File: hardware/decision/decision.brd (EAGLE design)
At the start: 45 x 70 mm, 8 parts, among them IC1 7805T, IC2 A1301UA

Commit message: update decision board with proper nets
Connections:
- removed net N$1: GND.1, GND.2, GND.3
- removed net N$2: VCC.1, VCC.2, VCC.3
- net GND: now also GND.1, GND.2, GND.3
- net VCC: now also VCC.1, VCC.2, VCC.3
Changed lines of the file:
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@@
 <contactref element="IC2" pad="2"/>
 <via x="2.54" y="13.97" extent="1-16" drill="1.4" diameter="2.54" shape="square"/>
+<contactref element="GND" pad="3"/>
+<contactref element="GND" pad="2"/>
+<contactref element="GND" pad="1"/>
 <wire x1="10.89" y1="18.86" x2="12.86" y2="53.51" width="0" layer="19" extent="1-1"/>
 <wire x1="2.54" y1="13.97" x2="10.89" y2="18.86" width="0" layer="19" extent="1-1"/>
 <wire x1="7.62" y1="6.35" x2="2.54" y2="13.97" width="0" layer="19" extent="1-1"/>
 <wire x1="13.97" y1="6.35" x2="7.62" y2="6.35" width="0" layer="19" extent="1-1"/>
+<wire x1="26.563" y1="6.41" x2="13.97" y2="6.35" width="0" layer="19" extent="1-1"/>
+<wire x1="26.817" y1="8.95" x2="26.563" y2="6.41" width="0" layer="19" extent="1-1"/>
+<wire x1="26.817" y1="3.87" x2="26.563" y2="6.41" width="0" layer="19" extent="1-1"/>
 </signal>
 <signal name="VCC">
@@
 <contactref element="C2" pad="1"/>
 <contactref element="IC2" pad="1"/>
+<contactref element="VCC" pad="1"/>
+<contactref element="VCC" pad="3"/>
+<contactref element="VCC" pad="2"/>
+<wire x1="13.43" y1="18.86" x2="12.86" y2="52.24" width="0" layer="19" extent="1-1"/>
 <wire x1="16.51" y1="6.35" x2="13.43" y2="18.86" width="0" layer="19" extent="1-1"/>
-<wire x1="12.86" y1="52.24" x2="16.51" y2="6.35" width="0" layer="19" extent="1-1"/>
+<wire x1="39.563" y1="6.49" x2="16.51" y2="6.35" width="0" layer="19" extent="1-1"/>
+<wire x1="39.817" y1="9.03" x2="39.563" y2="6.49" width="0" layer="19" extent="1-1"/>
+<wire x1="39.817" y1="3.95" x2="39.563" y2="6.49" width="0" layer="19" extent="1-1"/>
 </signal>
 <signal name="P1.2">
@@
 <wire x1="5.08" y1="6.35" x2="8.35" y2="18.86" width="0" layer="19" extent="1-1"/>
 </signal>
-<signal name="N$1">
-<contactref element="GND" pad="3"/>
-<contactref element="GND" pad="2"/>
-<contactref element="GND" pad="1"/>
-<wire x1="26.563" y1="6.41" x2="26.817" y2="8.95" width="0" layer="19" extent="1-1"/>
-<wire x1="26.817" y1="3.87" x2="26.563" y2="6.41" width="0" layer="19" extent="1-1"/>
-</signal>
-<signal name="N$2">
-<contactref element="VCC" pad="1"/>
-<contactref element="VCC" pad="3"/>
-<contactref element="VCC" pad="2"/>
-<wire x1="39.563" y1="6.49" x2="39.817" y2="9.03" width="0" layer="19" extent="1-1"/>
-<wire x1="39.817" y1="3.95" x2="39.563" y2="6.49" width="0" layer="19" extent="1-1"/>
-</signal>
 </signals>

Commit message: working on decision board traces
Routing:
- net N$3: track 0.00 -> 49.0 mm
- net N$5: track 0.00 -> 39.3 mm
- net N$2: track 0.00 -> 19.2 mm
- net N$1: track 0.00 -> 18.8 mm
- net N$4: track 0.00 -> 13.2 mm
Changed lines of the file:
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@@
 </signal>
 <signal name="9V">
-<via x="2.54" y="19.05" extent="1-16" drill="1.4" diameter="2.54" shape="square"/>
+<via x="2.54" y="18.05" extent="1-16" drill="1.4" diameter="2.54" shape="square"/>
 <contactref element="IC1" pad="1"/>
 <contactref element="C1" pad="2"/>
-<wire x1="2.54" y1="19.05" x2="8.35" y2="18.86" width="0" layer="19" extent="1-1"/>
+<wire x1="2.54" y1="18.05" x2="8.35" y2="18.86" width="0" layer="19" extent="1-1"/>
 <wire x1="5.08" y1="6.35" x2="8.35" y2="18.86" width="0" layer="19" extent="1-1"/>
 </signal>
+<signal name="N$3">
+<wire x1="13" y1="55" x2="13" y2="56" width="0.6096" layer="16"/>
+<wire x1="13" y1="56" x2="25" y2="68" width="0.6096" layer="16"/>
+<wire x1="25" y1="68" x2="40" y2="68" width="0.6096" layer="16"/>
+<wire x1="40" y1="68" x2="42" y2="66" width="0.6096" layer="16"/>
+<wire x1="42" y1="66" x2="42" y2="57" width="0.6096" layer="16"/>
+<wire x1="42" y1="57" x2="39" y2="54" width="0.6096" layer="16"/>
+</signal>
+<signal name="N$1">
+<wire x1="8" y1="18" x2="7" y2="18" width="0.8128" layer="16"/>
+<wire x1="7" y1="18" x2="5" y2="16" width="0.8128" layer="16"/>
+<wire x1="5" y1="16" x2="5" y2="6" width="0.8128" layer="16"/>
+<wire x1="7" y1="18" x2="2" y2="18" width="0.8128" layer="16"/>
+</signal>
+<signal name="N$2">
+<wire x1="11" y1="18" x2="11" y2="17" width="0.8128" layer="1"/>
+<wire x1="11" y1="17" x2="8" y2="14" width="0.8128" layer="1"/>
+<wire x1="8" y1="14" x2="2" y2="14" width="0.8128" layer="1"/>
+<wire x1="8" y1="14" x2="8" y2="6" width="0.8128" layer="1"/>
+</signal>
+<signal name="N$4">
+<wire x1="13" y1="18" x2="13" y2="13" width="0.8128" layer="1"/>
+<wire x1="13" y1="13" x2="16" y2="10" width="0.8128" layer="1"/>
+<wire x1="16" y1="10" x2="16" y2="6" width="0.8128" layer="1"/>
+</signal>
+<signal name="N$5">
+<wire x1="13" y1="20" x2="17" y2="20" width="0.6096" layer="1"/>
+<wire x1="17" y1="20" x2="19" y2="22" width="0.6096" layer="1"/>
+<wire x1="19" y1="22" x2="19" y2="46" width="0.6096" layer="1"/>
+<wire x1="19" y1="46" x2="13" y2="52" width="0.6096" layer="1"/>
+</signal>
 </signals>

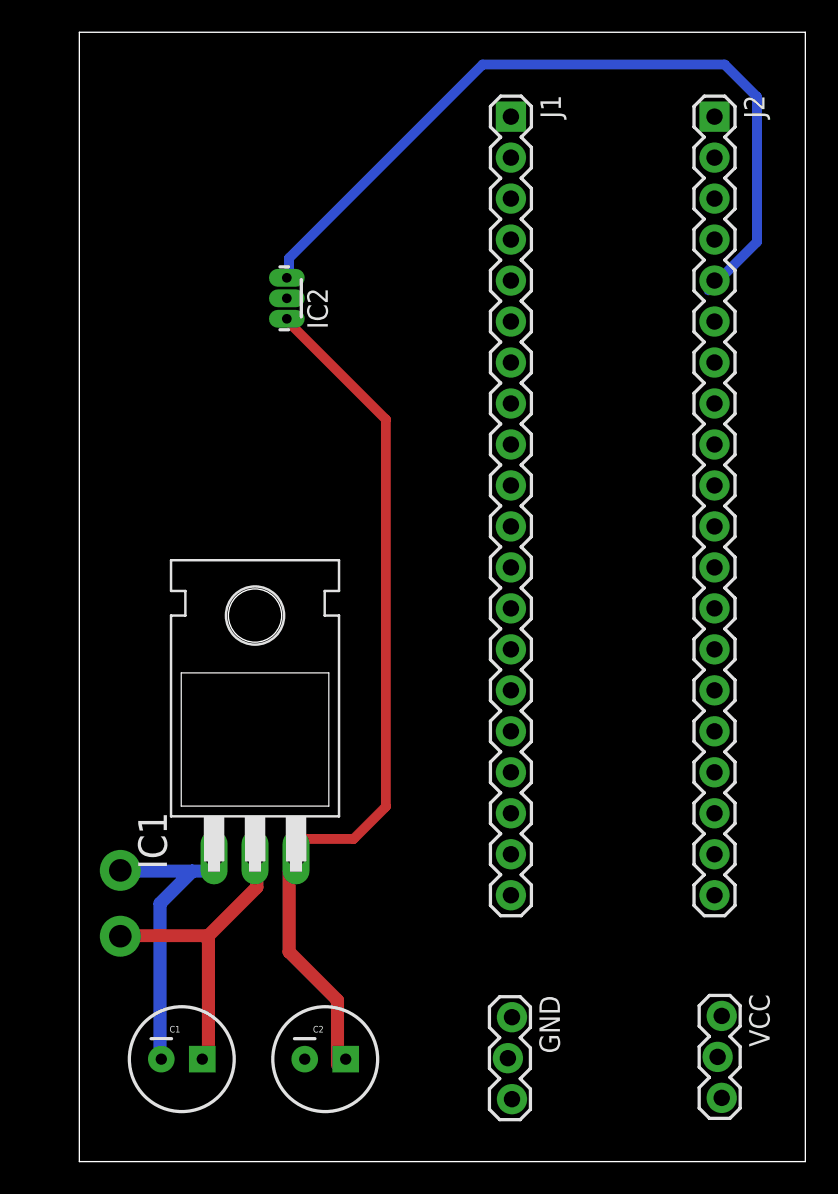
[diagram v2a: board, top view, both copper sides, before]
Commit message: update decision board with copper pools, silk screen, and proper routes
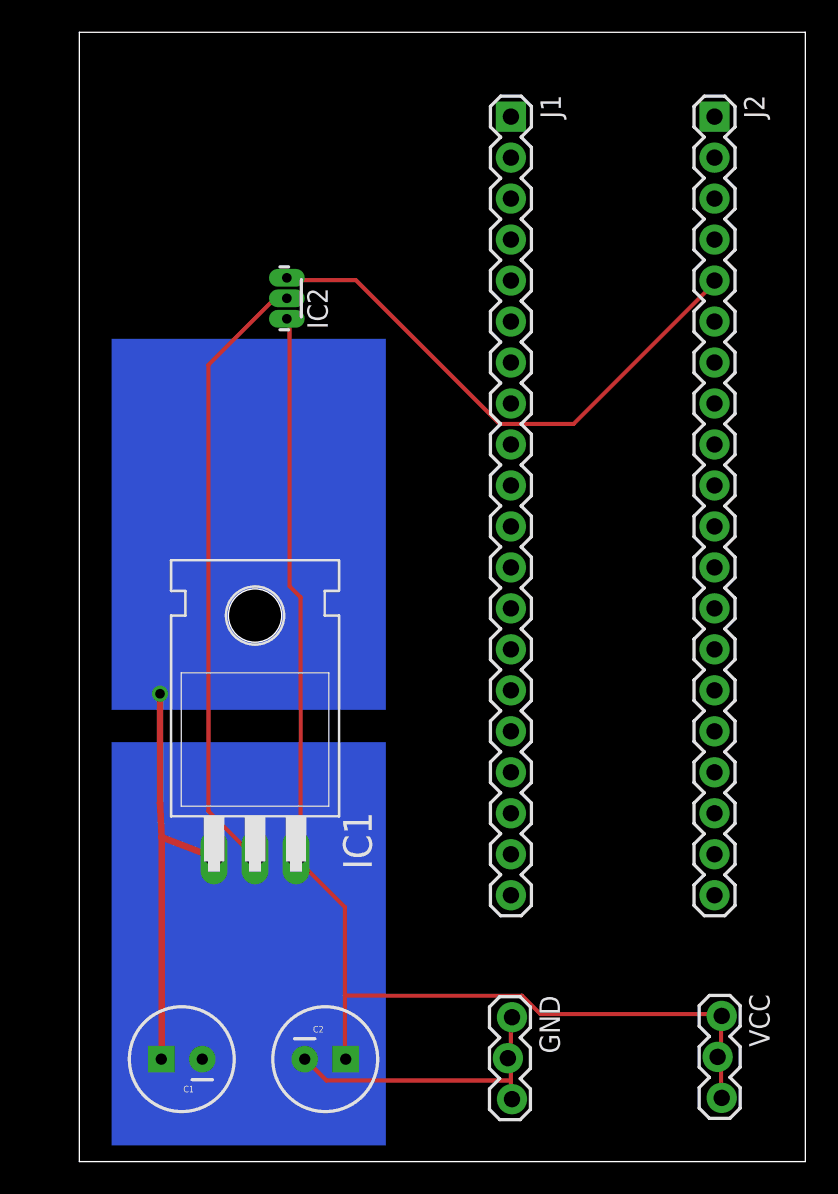
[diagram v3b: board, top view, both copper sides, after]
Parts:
- turned C1 to 180 degrees
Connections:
- net 9V: now also C1.1; no longer C1.2
- net GND: now also C1.2; no longer C1.1
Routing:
- net VCC: track 0.00 -> 76.9 mm
- net GND: track 0.00 -> 75.4 mm, vias 1 -> 0
- net N$3: track 49.0 -> 0.00 mm
- net N$5: track 39.3 -> 0.00 mm
- net P1.2: track 0.00 -> 34.0 mm
- net 9V: track 0.00 -> 26.1 mm
- net N$2: track 19.2 -> 0.00 mm
- net N$1: track 18.8 -> 0.00 mm
- net N$4: track 13.2 -> 0.00 mm
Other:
- board text added: "Decision Board"
- board text added: "Derailleurs"
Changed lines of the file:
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@@
 <wire x1="45" y1="70" x2="0" y2="70" width="0" layer="20"/>
 <wire x1="0" y1="70" x2="0" y2="0" width="0" layer="20"/>
+<rectangle x1="2" y1="1" x2="19" y2="26" layer="16"/>
+<text x="2" y="67" size="1.778" layer="48">Decision Board</text>
+<text x="2" y="64" size="1.778" layer="48">Derailleurs</text>
+<rectangle x1="2" y1="28" x2="19" y2="51" layer="16"/>
 </plain>
 <attributes>
@@
 <param name="RoutingGrid" value="50mil"/>
 <param name="AutoGrid" value="1"/>
-<param name="Efforts" value="0"/>
+<param name="Efforts" value="2"/>
 <param name="TopRouterVariant" value="1"/>
 <param name="tpViaShape" value="round"/>
@@
 </autorouter>
 <elements>
-<element name="C1" library="SparkFun-Capacitors" package="CPOL-RADIAL-100UF-25V" value="200µF" x="6.35" y="6.35"/>
+<element name="C1" library="SparkFun-Capacitors" package="CPOL-RADIAL-100UF-25V" value="200µF" x="6.35" y="6.35" rot="R180"/>
 <element name="C2" library="SparkFun-Capacitors" package="CPOL-RADIAL-100UF-25V" value="200µF" x="15.24" y="6.35"/>
 <element name="IC1" library="linear" package="TO220H" value="7805T" x="10.89" y="29.02"/>
@@
 <signal name="GND">
 <contactref element="IC1" pad="2"/>
-<contactref element="C1" pad="1"/>
+<contactref element="C1" pad="2"/>
 <contactref element="C2" pad="2"/>
 <contactref element="IC2" pad="2"/>
-<via x="2.54" y="13.97" extent="1-16" drill="1.4" diameter="2.54" shape="square"/>
 <contactref element="GND" pad="3"/>
 <contactref element="GND" pad="2"/>
 <contactref element="GND" pad="1"/>
-<wire x1="10.89" y1="18.86" x2="12.86" y2="53.51" width="0" layer="19" extent="1-1"/>
-<wire x1="2.54" y1="13.97" x2="10.89" y2="18.86" width="0" layer="19" extent="1-1"/>
-<wire x1="7.62" y1="6.35" x2="2.54" y2="13.97" width="0" layer="19" extent="1-1"/>
-<wire x1="13.97" y1="6.35" x2="7.62" y2="6.35" width="0" layer="19" extent="1-1"/>
-<wire x1="26.563" y1="6.41" x2="13.97" y2="6.35" width="0" layer="19" extent="1-1"/>
-<wire x1="26.817" y1="8.95" x2="26.563" y2="6.41" width="0" layer="19" extent="1-1"/>
-<wire x1="26.817" y1="3.87" x2="26.563" y2="6.41" width="0" layer="19" extent="1-1"/>
+<wire x1="10.89" y1="18.86" x2="10.89" y2="9.43" width="0.4064" layer="16"/>
+<wire x1="10.89" y1="9.43" x2="13.97" y2="6.35" width="0.4064" layer="16"/>
+<wire x1="10.89" y1="9.43" x2="10.7" y2="9.43" width="0.4064" layer="16"/>
+<wire x1="10.7" y1="9.43" x2="7.62" y2="6.35" width="0.4064" layer="16"/>
+<wire x1="26.7462" y1="8.9154" x2="26.7462" y2="6.6294" width="0.254" layer="1"/>
+<wire x1="26.7462" y1="6.6294" x2="26.563" y2="6.41" width="0.254" layer="1"/>
+<wire x1="26.7462" y1="8.9154" x2="26.817" y2="8.95" width="0.254" layer="1"/>
+<wire x1="26.7462" y1="6.4008" x2="26.7462" y2="5.0292" width="0.254" layer="1"/>
+<wire x1="26.7462" y1="5.0292" x2="26.7462" y2="3.8862" width="0.254" layer="1"/>
+<wire x1="26.7462" y1="3.8862" x2="26.817" y2="3.87" width="0.254" layer="1"/>
+<wire x1="26.7462" y1="6.4008" x2="26.563" y2="6.41" width="0.254" layer="1"/>
+<wire x1="12.1158" y1="53.4924" x2="12.8016" y2="53.4924" width="0.254" layer="1"/>
+<wire x1="8.001" y1="49.3776" x2="12.1158" y2="53.4924" width="0.254" layer="1"/>
+<wire x1="8.001" y1="21.717" x2="8.001" y2="49.3776" width="0.254" layer="1"/>
+<wire x1="10.7442" y1="18.9738" x2="8.001" y2="21.717" width="0.254" layer="1"/>
+<wire x1="12.8016" y1="53.4924" x2="12.86" y2="53.51" width="0.254" layer="1"/>
+<wire x1="10.7442" y1="18.9738" x2="10.89" y2="18.86" width="0.254" layer="1"/>
+<wire x1="15.3162" y1="5.0292" x2="26.7462" y2="5.0292" width="0.254" layer="1"/>
+<wire x1="14.1732" y1="6.1722" x2="15.3162" y2="5.0292" width="0.254" layer="1"/>
+<wire x1="14.1732" y1="6.1722" x2="13.97" y2="6.35" width="0.254" layer="1"/>
 </signal>
 <signal name="VCC">
@@
 <contactref element="VCC" pad="3"/>
 <contactref element="VCC" pad="2"/>
-<wire x1="13.43" y1="18.86" x2="12.86" y2="52.24" width="0" layer="19" extent="1-1"/>
-<wire x1="16.51" y1="6.35" x2="13.43" y2="18.86" width="0" layer="19" extent="1-1"/>
-<wire x1="39.563" y1="6.49" x2="16.51" y2="6.35" width="0" layer="19" extent="1-1"/>
-<wire x1="39.817" y1="9.03" x2="39.563" y2="6.49" width="0" layer="19" extent="1-1"/>
-<wire x1="39.817" y1="3.95" x2="39.563" y2="6.49" width="0" layer="19" extent="1-1"/>
+<wire x1="39.7764" y1="8.9154" x2="39.7764" y2="6.6294" width="0.254" layer="1"/>
+<wire x1="39.7764" y1="6.6294" x2="39.563" y2="6.49" width="0.254" layer="1"/>
+<wire x1="39.7764" y1="8.9154" x2="39.817" y2="9.03" width="0.254" layer="1"/>
+<wire x1="39.7764" y1="6.4008" x2="39.7764" y2="4.1148" width="0.254" layer="1"/>
+<wire x1="39.7764" y1="4.1148" x2="39.817" y2="3.95" width="0.254" layer="1"/>
+<wire x1="39.7764" y1="6.4008" x2="39.563" y2="6.49" width="0.254" layer="1"/>
+<wire x1="13.0302" y1="35.6616" x2="13.0302" y2="52.1208" width="0.254" layer="1"/>
+<wire x1="13.716" y1="34.9758" x2="13.0302" y2="35.6616" width="0.254" layer="1"/>
+<wire x1="13.716" y1="19.2024" x2="13.716" y2="34.9758" width="0.254" layer="1"/>
+<wire x1="13.4874" y1="18.9738" x2="13.716" y2="19.2024" width="0.254" layer="1"/>
+<wire x1="13.0302" y1="52.1208" x2="12.86" y2="52.24" width="0.254" layer="1"/>
+<wire x1="13.4874" y1="18.9738" x2="13.43" y2="18.86" width="0.254" layer="1"/>
+<wire x1="16.4592" y1="15.7734" x2="16.4592" y2="10.287" width="0.254" layer="1"/>
+<wire x1="16.4592" y1="10.287" x2="16.4592" y2="6.4008" width="0.254" layer="1"/>
+<wire x1="13.4874" y1="18.7452" x2="16.4592" y2="15.7734" width="0.254" layer="1"/>
+<wire x1="16.4592" y1="6.4008" x2="16.51" y2="6.35" width="0.254" layer="1"/>
+<wire x1="13.4874" y1="18.7452" x2="13.43" y2="18.86" width="0.254" layer="1"/>
+<wire x1="28.575" y1="9.144" x2="39.7764" y2="9.144" width="0.254" layer="1"/>
+<wire x1="27.432" y1="10.287" x2="28.575" y2="9.144" width="0.254" layer="1"/>
+<wire x1="16.4592" y1="10.287" x2="27.432" y2="10.287" width="0.254" layer="1"/>
+<wire x1="39.7764" y1="9.144" x2="39.817" y2="9.03" width="0.254" layer="1"/>
 </signal>
 <signal name="P1.2">
 <contactref element="IC2" pad="3"/>
 <contactref element="J2" pad="5"/>
-<wire x1="12.86" y1="54.78" x2="39.37" y2="54.61" width="0" layer="19" extent="1-1"/>
+<wire x1="17.145" y1="54.6354" x2="13.0302" y2="54.6354" width="0.254" layer="1"/>
+<wire x1="26.0604" y1="45.72" x2="17.145" y2="54.6354" width="0.254" layer="1"/>
+<wire x1="30.6324" y1="45.72" x2="26.0604" y2="45.72" width="0.254" layer="1"/>
+<wire x1="39.3192" y1="54.4068" x2="30.6324" y2="45.72" width="0.254" layer="1"/>
+<wire x1="13.0302" y1="54.6354" x2="12.86" y2="54.78" width="0.254" layer="1"/>
+<wire x1="39.3192" y1="54.4068" x2="39.37" y2="54.61" width="0.254" layer="1"/>
 </signal>
 <signal name="9V">
-<via x="2.54" y="18.05" extent="1-16" drill="1.4" diameter="2.54" shape="square"/>
 <contactref element="IC1" pad="1"/>
-<contactref element="C1" pad="2"/>
-<wire x1="2.54" y1="18.05" x2="8.35" y2="18.86" width="0" layer="19" extent="1-1"/>
-<wire x1="5.08" y1="6.35" x2="8.35" y2="18.86" width="0" layer="19" extent="1-1"/>
-</signal>
-<signal name="N$3">
-<wire x1="13" y1="55" x2="13" y2="56" width="0.6096" layer="16"/>
-<wire x1="13" y1="56" x2="25" y2="68" width="0.6096" layer="16"/>
-<wire x1="25" y1="68" x2="40" y2="68" width="0.6096" layer="16"/>
-<wire x1="40" y1="68" x2="42" y2="66" width="0.6096" layer="16"/>
-<wire x1="42" y1="66" x2="42" y2="57" width="0.6096" layer="16"/>
-<wire x1="42" y1="57" x2="39" y2="54" width="0.6096" layer="16"/>
-</signal>
-<signal name="N$1">
-<wire x1="8" y1="18" x2="7" y2="18" width="0.8128" layer="16"/>
-<wire x1="7" y1="18" x2="5" y2="16" width="0.8128" layer="16"/>
-<wire x1="5" y1="16" x2="5" y2="6" width="0.8128" layer="16"/>
-<wire x1="7" y1="18" x2="2" y2="18" width="0.8128" layer="16"/>
-</signal>
-<signal name="N$2">
-<wire x1="11" y1="18" x2="11" y2="17" width="0.8128" layer="1"/>
-<wire x1="11" y1="17" x2="8" y2="14" width="0.8128" layer="1"/>
-<wire x1="8" y1="14" x2="2" y2="14" width="0.8128" layer="1"/>
-<wire x1="8" y1="14" x2="8" y2="6" width="0.8128" layer="1"/>
-</signal>
-<signal name="N$4">
-<wire x1="13" y1="18" x2="13" y2="13" width="0.8128" layer="1"/>
-<wire x1="13" y1="13" x2="16" y2="10" width="0.8128" layer="1"/>
-<wire x1="16" y1="10" x2="16" y2="6" width="0.8128" layer="1"/>
-</signal>
-<signal name="N$5">
-<wire x1="13" y1="20" x2="17" y2="20" width="0.6096" layer="1"/>
-<wire x1="17" y1="20" x2="19" y2="22" width="0.6096" layer="1"/>
-<wire x1="19" y1="22" x2="19" y2="46" width="0.6096" layer="1"/>
-<wire x1="19" y1="46" x2="13" y2="52" width="0.6096" layer="1"/>
+<contactref element="C1" pad="1"/>
+<wire x1="8.35" y1="18.86" x2="5.105" y2="20.105" width="0.4064" layer="1"/>
+<wire x1="5.105" y1="20.105" x2="5" y2="22.21" width="0.4064" layer="1"/>
+<wire x1="5" y1="22.21" x2="5" y2="29" width="0.4064" layer="1"/>
+<via x="5" y="29" extent="1-16" drill="0.6" shape="square"/>
+<wire x1="5.08" y1="6.35" x2="5.105" y2="6.375" width="0.4064" layer="1"/>
+<wire x1="5.105" y1="6.375" x2="5.105" y2="20.105" width="0.4064" layer="1"/>
 </signal>
 </signals>

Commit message: finish boards
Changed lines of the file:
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@@
 <wire x1="0" y1="70" x2="0" y2="0" width="0" layer="20"/>
 <rectangle x1="2" y1="1" x2="19" y2="26" layer="16"/>
-<text x="2" y="67" size="1.778" layer="48">Decision Board</text>
-<text x="2" y="64" size="1.778" layer="48">Derailleurs</text>
+<text x="2" y="67" size="1.778" layer="112">Decision Board</text>
+<text x="2" y="64" size="1.778" layer="112">Derailleurs</text>
 <rectangle x1="2" y1="28" x2="19" y2="51" layer="16"/>
 </plain>
